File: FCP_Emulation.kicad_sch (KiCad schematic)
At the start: 112 parts, among them J1 Conn_01x10_Female, J2 Conn_01x10_Female, J3 Conn_01x10_Female, J4 Conn_01x02_Female, J5 Conn_01x02_Female, Q1 PMOS, U1 LM2904, U10 LM2904, U11 LM2904, U12 LM2904, U13 LM2904, U14 LM2904, U15 LM2904, U16 LM2904, U17 LM2904, U2 LM2904, U4 LM2904, U6 LM2904, U7 LM2904, U8 LM2904, U9 LM2904

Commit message: Added datasheets and footprints to most components
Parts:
- C10: footprint Capacitor_Tantalum_SMD:CP_EIA-3216-10_Kemet-I -> Capacitor_SMD:C_0603_1608Metric
- C7, C9: footprint (none) -> Capacitor_SMD:CP_Elec_10x10.5
- R57, R58, R59, R74: footprint Resistor_SMD:R_01005_0402Metric -> Resistor_SMD:R_0603_1608Metric
- R70: footprint Resistor_SMD:R_0402_1005Metric -> Resistor_SMD:R_0603_1608Metric
- R72: footprint (none) -> Resistor_SMD:R_0603_1608Metric
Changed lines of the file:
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@@
       (effects (font (size 1.27 1.27)))
     )
-    (property "Footprint" "Resistor_SMD:R_01005_0402Metric" (at 78.74 225.552 90)
+    (property "Footprint" "Resistor_SMD:R_0603_1608Metric" (at 78.74 225.552 90)
       (effects (font (size 1.27 1.27)) hide)
     )
@@
       (effects (font (size 1.27 1.27)) (justify left))
     )
-    (property "Footprint" "Resistor_SMD:R_01005_0402Metric" (at 117.602 205.74 90)
+    (property "Footprint" "Resistor_SMD:R_0603_1608Metric" (at 117.602 205.74 90)
       (effects (font (size 1.27 1.27)) hide)
     )
@@
       (effects (font (size 1.27 1.27)))
     )
-    (property "Footprint" "Resistor_SMD:R_01005_0402Metric" (at 116.84 257.302 90)
+    (property "Footprint" "Resistor_SMD:R_0603_1608Metric" (at 116.84 257.302 90)
       (effects (font (size 1.27 1.27)) hide)
     )
@@
       (effects (font (size 1.27 1.27)) (justify right))
     )
-    (property "Footprint" "" (at 231.14 59.69 0)
+    (property "Footprint" "Capacitor_SMD:CP_Elec_10x10.5" (at 231.14 59.69 0)
       (effects (font (size 1.27 1.27)) hide)
     )
-    (property "Datasheet" "~" (at 231.14 59.69 0)
+    (property "Datasheet" "https://api.pim.na.industrial.panasonic.com/file_stream/main/fileversion/3101" (at 231.14 59.69 0)
       (effects (font (size 1.27 1.27)) hide)
     )
@@
       (effects (font (size 1.27 1.27)) (justify right))
     )
-    (property "Footprint" "" (at 223.52 91.44 0)
+    (property "Footprint" "Capacitor_SMD:CP_Elec_10x10.5" (at 223.52 91.44 0)
       (effects (font (size 1.27 1.27)) hide)
     )
-    (property "Datasheet" "~" (at 223.52 91.44 0)
+    (property "Datasheet" "https://api.pim.na.industrial.panasonic.com/file_stream/main/fileversion/3101" (at 223.52 91.44 0)
       (effects (font (size 1.27 1.27)) hide)
     )
@@
       (effects (font (size 1.27 1.27)) hide)
     )
-    (property "Datasheet" "~" (at 227.33 74.93 0)
+    (property "Datasheet" "https://products.sumida.com/products/pdf/CDPH4D19F.pdf" (at 227.33 74.93 0)
       (effects (font (size 1.27 1.27)) hide)
     )
@@
       (effects (font (size 1.27 1.27)) (justify left))
     )
-    (property "Footprint" "Capacitor_Tantalum_SMD:CP_EIA-3216-10_Kemet-I" (at 227.33 84.1248 0)
+    (property "Footprint" "Capacitor_SMD:C_0603_1608Metric" (at 227.33 84.1248 0)
       (effects (font (size 1.27 1.27)) hide)
     )
-    (property "Datasheet" "https://datasheets.kyocera-avx.com/TAJ.pdf" (at 223.52 85.09 0)
+    (property "Datasheet" "https://mm.digikey.com/Volume0/opasdata/d220001/medias/docus/658/CL10B104KB8NNWC_Spec.pdf" (at 223.52 85.09 0)
       (effects (font (size 1.27 1.27)) hide)
     )
@@
       (effects (font (size 1.27 1.27)) (justify left))
     )
-    (property "Footprint" "Resistor_SMD:R_01005_0402Metric" (at 118.872 251.46 90)
+    (property "Footprint" "Resistor_SMD:R_0603_1608Metric" (at 118.872 251.46 90)
       (effects (font (size 1.27 1.27)) hide)
     )
@@
       (effects (font (size 1.27 1.27)))
     )
-    (property "Footprint" "" (at 259.08 100.838 90)
+    (property "Footprint" "Resistor_SMD:R_0603_1608Metric" (at 259.08 100.838 90)
       (effects (font (size 1.27 1.27)) hide)
     )
-    (property "Datasheet" "~" (at 259.08 99.06 0)
+    (property "Datasheet" "https://www.passivecomponent.com/wp-content/uploads/chipR/ASC_WR.pdf" (at 259.08 99.06 0)
       (effects (font (size 1.27 1.27)) hide)
     )
@@
       (effects (font (size 1.27 1.27)))
     )
-    (property "Footprint" "Resistor_SMD:R_0402_1005Metric" (at 247.65 100.838 90)
+    (property "Footprint" "Resistor_SMD:R_0603_1608Metric" (at 247.65 100.838 90)
       (effects (font (size 1.27 1.27)) hide)
     )
-    (property "Datasheet" "https://api.pim.na.industrial.panasonic.com/file_stream/main/fileversion/1242" (at 247.65 99.06 0)
+    (property "Datasheet" "https://www.seielect.com/catalog/sei-rmcf_rmcp.pdf" (at 247.65 99.06 0)
       (effects (font (size 1.27 1.27)) hide)
     )

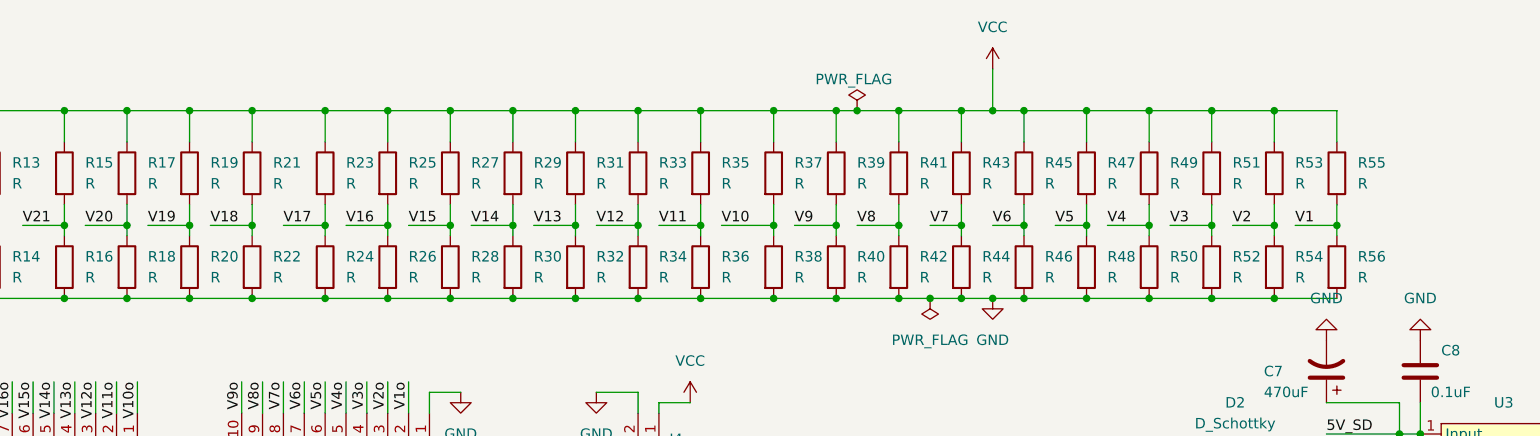
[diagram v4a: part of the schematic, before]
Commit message: added inductor footprints and resistor values
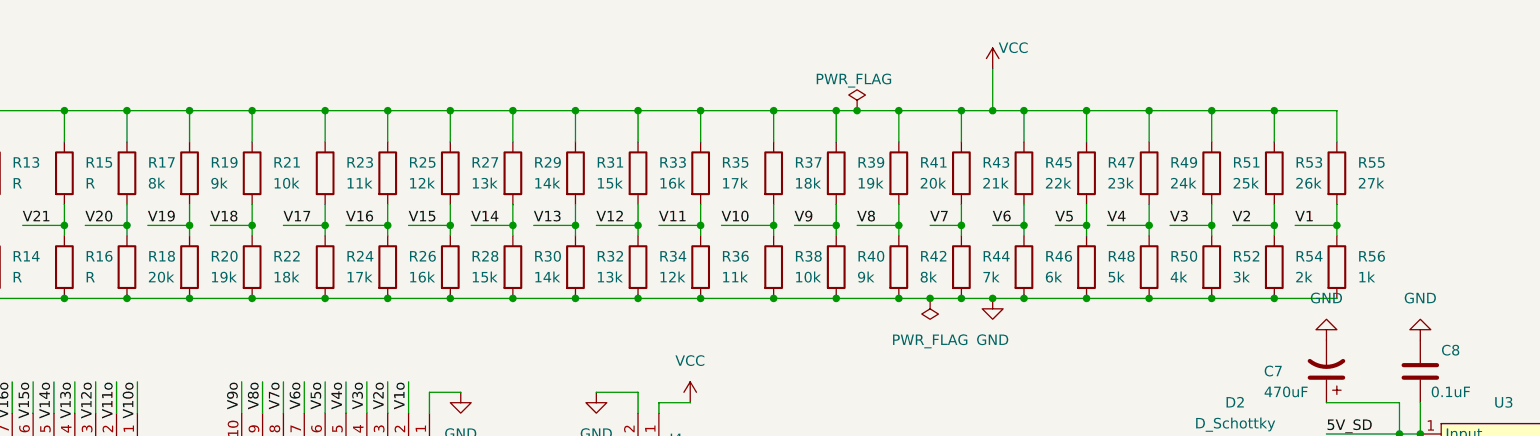
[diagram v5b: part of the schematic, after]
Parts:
- L1, L2: footprint (none) -> sumida_inductor_footprint:L_Sumida_CDPH4D19F
- R17, R42: value R -> 8k
- R18, R41: value R -> 20k
- R19, R40: value R -> 9k
- R20, R39: value R -> 19k
- R21, R38: value R -> 10k
- R22, R37: value R -> 18k
- R23, R36: value R -> 11k
- R24, R35: value R -> 17k
- R25, R34: value R -> 12k
- R26, R33: value R -> 16k
- R27, R32: value R -> 13k
- R28, R31: value R -> 15k
- R29, R30: value R -> 14k
- R43: value R -> 21k
- R44: value R -> 7k
- R45: value R -> 22k
- R46: value R -> 6k
- R47: value R -> 23k
- R48: value R -> 5k
- R49: value R -> 24k
- R50: value R -> 4k
- R51: value R -> 25k
- R52: value R -> 3k
- R53: value R -> 26k
- R54: value R -> 2k
- R55: value R -> 27k
- R56: value R -> 1k

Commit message: resistor grid specced but still have to double check connections
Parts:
- removed R32: 13k, Resistor_SMD:R_0805_2012Metric, symbol Device:R
- removed R49: 24k, Resistor_SMD:R_0805_2012Metric, symbol Device:R
- removed R50: 4k, Resistor_SMD:R_0805_2012Metric, symbol Device:R
- removed R51: 25k, Resistor_SMD:R_0805_2012Metric, symbol Device:R
- removed R52: 3k, Resistor_SMD:R_0805_2012Metric, symbol Device:R
- removed R53: 26k, Resistor_SMD:R_0805_2012Metric, symbol Device:R
- removed R54: 2k, Resistor_SMD:R_0805_2012Metric, symbol Device:R
- removed R55: 27k, Resistor_SMD:R_0805_2012Metric, symbol Device:R
- removed R56: 1k, Resistor_SMD:R_0805_2012Metric, symbol Device:R
- removed U12, U15: LM2904, symbol Amplifier_Operational:LM2904
- R1, R11, R15, R3, R5, R7: value R -> 1K; footprint Resistor_SMD:R_0805_2012Metric -> Resistor_SMD:R_0603_1608Metric
- R10: value R -> 19K; footprint Resistor_SMD:R_0805_2012Metric -> Resistor_SMD:R_0603_1608Metric
- R12: value R -> 3K; footprint Resistor_SMD:R_0805_2012Metric -> Resistor_SMD:R_0603_1608Metric
- R13, R6: value R -> 7K; footprint Resistor_SMD:R_0805_2012Metric -> Resistor_SMD:R_0603_1608Metric
- R14: value R -> 17K; footprint Resistor_SMD:R_0805_2012Metric -> Resistor_SMD:R_0603_1608Metric
- R16: value R -> 2K; footprint Resistor_SMD:R_0805_2012Metric -> Resistor_SMD:R_0603_1608Metric
- R17: value 8k -> 3K; footprint Resistor_SMD:R_0805_2012Metric -> Resistor_SMD:R_0603_1608Metric
- R18, R41: value 20k -> 5K; footprint Resistor_SMD:R_0805_2012Metric -> Resistor_SMD:R_0603_1608Metric
- R19, R40: value 9k -> 5K; footprint Resistor_SMD:R_0805_2012Metric -> Resistor_SMD:R_0603_1608Metric
- R2: value R -> 22.9K; footprint Resistor_SMD:R_0805_2012Metric -> Resistor_SMD:R_0603_1608Metric
- R20: value 19k -> 7K; footprint Resistor_SMD:R_0805_2012Metric -> Resistor_SMD:R_0603_1608Metric
- R21: value 10k -> 11K; footprint Resistor_SMD:R_0805_2012Metric -> Resistor_SMD:R_0603_1608Metric
- R22: value 18k -> 13K; footprint Resistor_SMD:R_0805_2012Metric -> Resistor_SMD:R_0603_1608Metric
- R23: value 11k -> 1K; footprint Resistor_SMD:R_0805_2012Metric -> Resistor_SMD:R_0603_1608Metric
- R24: value 17k -> 1K; footprint Resistor_SMD:R_0805_2012Metric -> Resistor_SMD:R_0603_1608Metric
- R25: value 12k -> 13K; footprint Resistor_SMD:R_0805_2012Metric -> Resistor_SMD:R_0603_1608Metric
- R26: value 16k -> 11K; footprint Resistor_SMD:R_0805_2012Metric -> Resistor_SMD:R_0603_1608Metric
- R27: value 13k -> 7K; footprint Resistor_SMD:R_0805_2012Metric -> Resistor_SMD:R_0603_1608Metric
- R28: value 15k -> 5K; footprint Resistor_SMD:R_0805_2012Metric -> Resistor_SMD:R_0603_1608Metric
- R29: value 14k -> 5K; footprint Resistor_SMD:R_0805_2012Metric -> Resistor_SMD:R_0603_1608Metric
- R30: value 14k -> 3K; footprint Resistor_SMD:R_0805_2012Metric -> Resistor_SMD:R_0603_1608Metric
- R31: value 15k -> 1K; footprint Resistor_SMD:R_0805_2012Metric -> Resistor_SMD:R_0603_1608Metric
- R33: value 16k -> 2K; footprint Resistor_SMD:R_0805_2012Metric -> Resistor_SMD:R_0603_1608Metric
- R34: value 12k -> 1K; footprint Resistor_SMD:R_0805_2012Metric -> Resistor_SMD:R_0603_1608Metric
- R35, R39: footprint Resistor_SMD:R_0805_2012Metric -> Resistor_SMD:R_0603_1608Metric
- R36: value 11k -> 7K; footprint Resistor_SMD:R_0805_2012Metric -> Resistor_SMD:R_0603_1608Metric
- R37: value 18k -> 3K; footprint Resistor_SMD:R_0805_2012Metric -> Resistor_SMD:R_0603_1608Metric
- R38: value 10k -> 1K; footprint Resistor_SMD:R_0805_2012Metric -> Resistor_SMD:R_0603_1608Metric
- R4: value R -> 11K; footprint Resistor_SMD:R_0805_2012Metric -> Resistor_SMD:R_0603_1608Metric
- R42: value 8k -> 1K; footprint Resistor_SMD:R_0805_2012Metric -> Resistor_SMD:R_0603_1608Metric
- R43: value 21k -> 7K; footprint Resistor_SMD:R_0805_2012Metric -> Resistor_SMD:R_0603_1608Metric
- R44: value 7k -> 1K; footprint Resistor_SMD:R_0805_2012Metric -> Resistor_SMD:R_0603_1608Metric
- R45: value 22k -> 11K; footprint Resistor_SMD:R_0805_2012Metric -> Resistor_SMD:R_0603_1608Metric
- R46: value 6k -> 1K; footprint Resistor_SMD:R_0805_2012Metric -> Resistor_SMD:R_0603_1608Metric
- R47: value 23k -> 22.9K; footprint Resistor_SMD:R_0805_2012Metric -> Resistor_SMD:R_0603_1608Metric
- R48: value 5k -> 1K; footprint Resistor_SMD:R_0805_2012Metric -> Resistor_SMD:R_0603_1608Metric
- R8, R9: value R -> 5K; footprint Resistor_SMD:R_0805_2012Metric -> Resistor_SMD:R_0603_1608Metric
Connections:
- net V25 is gone; now on net V20: R7.2, R8.1
- net V26 is gone; now on net V21: R5.2, R6.1
- net V27 is gone; now on net V22: R3.2, R4.1
- net V28 is gone; now on net V23: R1.2, R2.1
- net GND: now also R31.2
- net V1: now also R47.2, R48.1
- net V10: now also R27.2, R28.1; no longer R37.2, R38.1
- net V11: now also R25.2, R26.1; no longer R35.2, R36.1
- net V12: now also R23.2, R24.1; no longer R33.2, R34.1
- net V13: now also R21.2, R22.1; no longer R31.2
- net V14: now also R19.2, R20.1; no longer R29.2, R30.1
- net V15: now also R17.2, R18.1; no longer R27.2, R28.1
- net V16: now also R15.2, R16.1; no longer R25.2, R26.1
- net V17: now also R13.2, R14.1; no longer R23.2, R24.1
- net V18: now also R11.2, R12.1; no longer R21.2, R22.1
- net V19: now also R10.1, R9.2; no longer R19.2, R20.1
- net V2: now also R45.2, R46.1
- net V20: no longer R17.2, R18.1
- net V21: no longer R15.2, R16.1
- net V22: no longer R13.2, R14.1
- net V23: no longer R11.2, R12.1
- net V3: now also R43.2, R44.1
- net V4: now also R41.2, R42.1
- net V5: now also R39.2, R40.1; no longer R47.2, R48.1
- net V6: now also R37.2, R38.1; no longer R45.2, R46.1
- net V7: now also R35.2, R36.1; no longer R43.2, R44.1
- net V8: now also R33.2, R34.1; no longer R41.2, R42.1
- net V9: now also R29.2, R30.1; no longer R39.2, R40.1
- net VCC: now also U11.5 (+)
- removed net V24: R10.1, R9.2, U11.5 (+)
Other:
- moved on the sheet: A1, C1, C10, C2, C3, C4, C5, C6, C7, C8, C9, CS8-5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

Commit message: ok ive updated the connections but someone shld really look this over
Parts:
- removed J1: Conn_01x10_Female, Connector_Phoenix_MC:PhoenixContact_MCV_1,5_10-G-3.5_1x10_P3.50mm_Vertical, symbol Connector:Conn_01x10_Female
- removed unit 2 of U4
- added J6: Conn_01x06_Socket, symbol Connector:Conn_01x06_Socket
- added unit 3 of U3
- added unit 3 of U5
- renumbered U1 to U3, U2 to U5
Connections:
- net +1V0: no longer U1.8 (V+), U2.8 (V+)
- net GND: no longer U1.4 (V-)
- net Out_0.5: now also J3.2 (Pin_2), U2.1, U2.2 (-); no longer J3.3 (Pin_3), U2.6 (-), U2.7
- net Out_0.7: now also J3.3 (Pin_3); no longer J3.4 (Pin_4)
- net V1: now also U1.4 (V-), U2.8 (V+)
- net V2: now also U1.8 (V+), U3.4 (V-)
- net V20o: now also J6.1 (Pin_1)
- net V21o: now also J6.2 (Pin_2)
- net V22o: now also J6.3 (Pin_3)
- net V23o: now also J6.4 (Pin_4)
- net V24o: now also J6.5 (Pin_5)
- net V3: now also U3.8 (V+), U5.4 (V-)
- net V4: now also U5.8 (V+)
- net V5: now also U2.3 (+), U3.3 (+); no longer U2.5 (+), U3.5 (+)
- net VCCo: now also J6.6 (Pin_6)
- removed net Out_0.75: J3.5 (Pin_5), U3.6 (-), U3.7
- net V1o renamed V4o
- net V4o: now also J3.5 (Pin_5); no longer J3.2 (Pin_2)
- new net V3o: J3.4 (Pin_4), U3.1, U3.2 (-)
- no-connect marks 27 -> 24
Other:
- moved on the sheet: U1C

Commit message: added op amp power connector and changed op amp power source. pwm case needs to be checked
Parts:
- added J1: Conn_01x02_Female, Connector_Molex:Molex_Mini-Fit_Jr_5569-02A2_2x01_P4.20mm_Horizontal, symbol Connector:Conn_01x02_Female
- renumbered U3 to B1
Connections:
- net VCCo is gone; now on net VCC: J6.6 (Pin_6)
- net +1V0: no longer U10.8 (V+), U11.8 (V+), U13.8 (V+), U14.8 (V+), U16.8 (V+), U17.8 (V+), U4.8 (V+), U6.8 (V+), U7.8 (V+), U8.8 (V+), U9.8 (V+)
- net GND: now also J1.2 (Pin_2)
- new net 30V: J1.1 (Pin_1), U10.8 (V+), U11.8 (V+), U13.8 (V+), U14.8 (V+), U16.8 (V+), U17.8 (V+), U4.8 (V+), U6.8 (V+), U7.8 (V+), U8.8 (V+), U9.8 (V+)
